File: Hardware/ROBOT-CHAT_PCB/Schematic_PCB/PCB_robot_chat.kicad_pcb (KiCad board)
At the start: 4 copper layers, 67 x 57 mm, 94 parts, among them J1 Conn_01x04, J10 Conn_01x02, J11 Conn_01x02, J12 Conn_01x02, J201 Conn_ST_STDC14, J3 Conn_01x02, J4 Conn_01x02, J5 Conn_01x02, J6 Conn_01x02, J7 Conn_01x06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

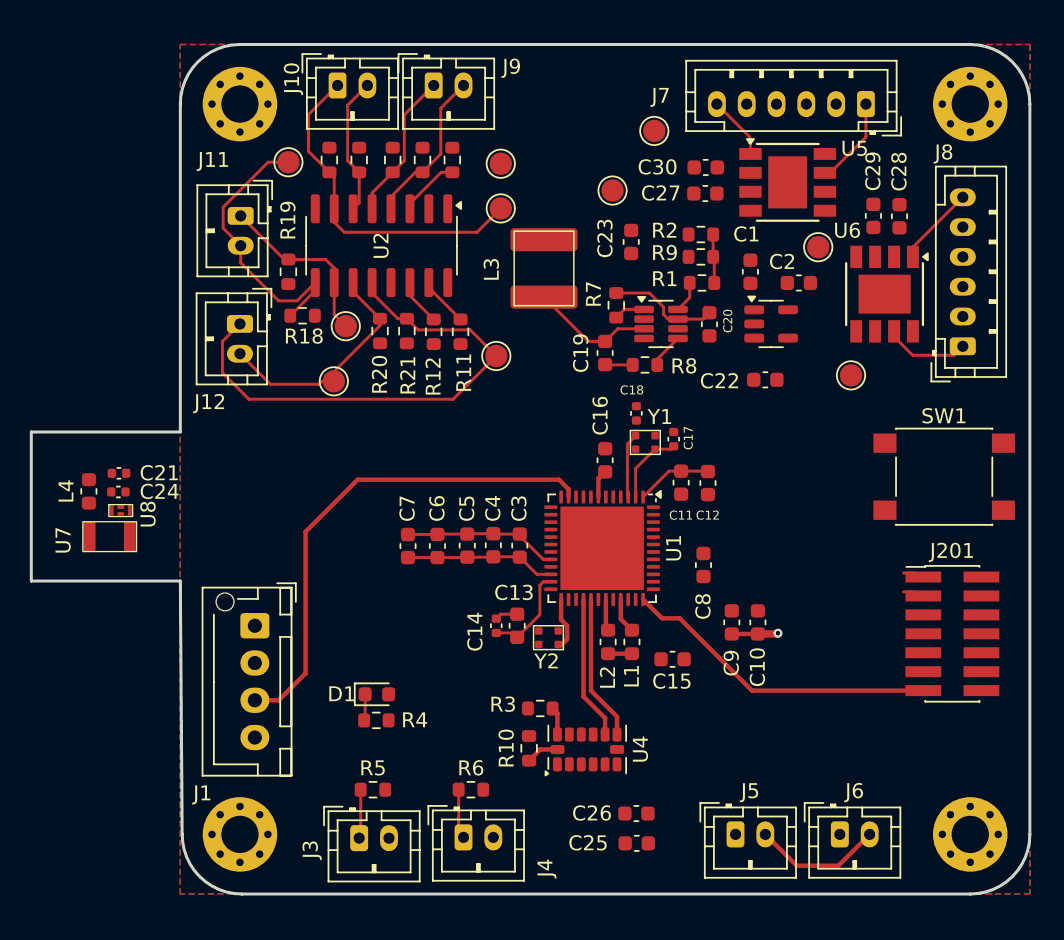
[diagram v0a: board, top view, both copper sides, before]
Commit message: Rerouting avec Mr Fiack
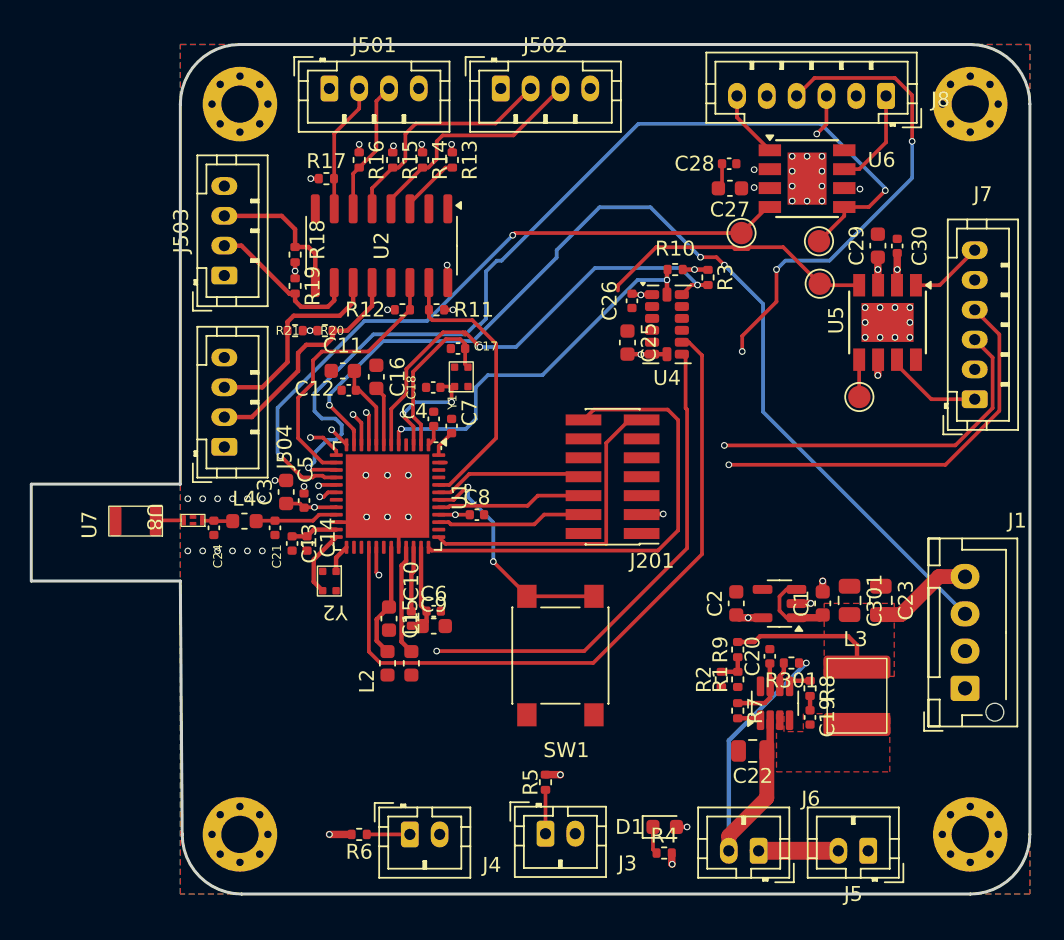
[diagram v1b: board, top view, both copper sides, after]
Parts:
- removed J10, J11, J12, J9: Conn_01x02, Connector_JST:JST_PH_B2B-PH-K_1x02_P2.00mm_Vertical
- removed TP1, TP2, TP3, TP4, TP5, TP6: TestPoint_Small, TestPoint:TestPoint_Pad_D1.5mm
- added C301: 22u, Capacitor_SMD:C_0805_2012Metric, F.Cu at (153.9, 66.3)
- added J501: Conn_01x04, Connector_JST:JST_PH_B4B-PH-K_1x04_P2.00mm_Vertical, F.Cu at (119.0, 31.9)
- added J502: Conn_01x04, Connector_JST:JST_PH_B4B-PH-K_1x04_P2.00mm_Vertical, F.Cu at (130.5, 31.9)
- added J503: Conn_01x04, Connector_JST:JST_PH_B4B-PH-K_1x04_P2.00mm_Vertical, F.Cu at (112.0, 44.5)
- added J504: Conn_01x04, Connector_JST:JST_PH_B4B-PH-K_1x04_P2.00mm_Vertical, F.Cu at (112.0, 56.0)
- added R301: 100k, Resistor_SMD:R_0402_1005Metric, F.Cu at (150.0, 70.5)
- C10, C13, C4, C5, C6, C7, C8: value 100nF -> 100n; footprint Capacitor_SMD:C_0603_1608Metric -> Capacitor_SMD:C_0402_1005Metric
- C12, C28, C30: footprint Capacitor_SMD:C_0603_1608Metric -> Capacitor_SMD:C_0402_1005Metric
- C19, C20: value 0,1uF -> 100n; footprint Capacitor_SMD:C_0603_1608Metric -> Capacitor_SMD:C_0402_1005Metric
- C22: footprint Capacitor_SMD:C_0603_1608Metric -> Capacitor_SMD:C_0805_2012Metric
- C23: value 47uF -> 22u; footprint Capacitor_SMD:C_0603_1608Metric -> Capacitor_SMD:C_0805_2012Metric
- C26: value 0.1uF -> 100n; footprint Capacitor_SMD:C_0603_1608Metric -> Capacitor_SMD:C_0402_1005Metric
- L3: value 4,7uH -> 4.7uH
- R1, R10, R11, R12, R13, R14, R15, R16, R17, R18, R19, R2, R20, R21, R3, R4, R5, R6, R7, R8: footprint Resistor_SMD:R_0603_1608Metric -> Resistor_SMD:R_0402_1005Metric
- R9: value 40,2k -> 40.2k; footprint Resistor_SMD:R_0603_1608Metric -> Resistor_SMD:R_0402_1005Metric
- moved J1 47.8 mm to (161.7, 72.2), turned to 90 degrees
- moved L3 35.5 mm to (150.9, 72.8)
- moved C26 34.4 mm to (139.3, 46.2), turned to -90 degrees
- moved C25 33.6 mm to (139.0, 49.0), turned to -90 degrees
- moved R10 33.6 mm to (142.2, 44.1), turned to 180 degrees
- moved R3 31.0 mm to (144.4, 44.6), turned to -90 degrees
- moved R2 29.9 mm to (145.3, 71.6), turned to 90 degrees
- moved C23 29.3 mm to (156.0, 66.3), turned to -90 degrees
- moved U4 29.0 mm to (141.7, 47.8), turned to 0 degrees
- moved SW1 28.4 mm to (134.5, 70.0), turned to -90 degrees
- moved R7 28.4 mm to (146.4, 73.7)
- moved C19 28.1 mm to (151.2, 74.2), turned to -90 degrees
- moved R1 26.7 mm to (146.4, 71.6), turned to 90 degrees
- moved MP1475DJ-LF-P1 26.6 mm to (148.9, 73.2), turned to 90 degrees
- moved R9 26.5 mm to (146.4, 69.6), turned to 90 degrees
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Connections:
- net Net-(MP1475DJ-LF-P1-BST) renamed /Power/BST
- net Net-(MP1475DJ-LF-P1-FB) renamed /Power/FB
- net Net-(MP1475DJ-LF-P1-PG) renamed /Power/PG
- net Net-(MP1475DJ-LF-P1-SW) renamed /Power/SW
- net Net-(MP1475DJ-LF-P1-VCC) renamed /Power/VCC
- C8 pad 1: +5V -> +3.3V
- J6 pad 1: +7.2V -> /Power/Vbatt+
- J6 pad 2: /Power/Vbatt+ -> +7.2V
- MP1475DJ-LF-P1 pad 6: +5V -> /Power/EN
- U1 pad 12: unconnected-(U1-PA3-Pad12) -> /STM/STATUS_LEDV
- U1 pad 13: /Driver/FWD_2 -> /STM/STATUS_LEDR
- U1 pad 14: /Driver/FWD_1 -> /Multiplexeur/SCL
- U1 pad 15: /Driver/REV_1 -> /Driver/REV_2
- U1 pad 16: /Multiplexeur/SCL -> /Driver/FWD_2
- U1 pad 17: /Driver/REV_2 -> /Driver/Encodeur_2A
- U1 pad 18: /STM/VCP_TX -> /Driver/Encodeur_2B
- U1 pad 36: /STM/VCP_RX -> /STM/VCP_TX
- U1 pad 37: /Driver/Encodeur_2A -> /STM/VCP_RX
- U1 pad 38: /Driver/Encodeur_2B -> unconnected-(U1-PA12-Pad38)
- U1 pad 40: +5V -> +3.3V
- U1 pad 46: /STM/STATUS_LEDV -> /Driver/REV_1
- U1 pad 47: /STM/STATUS_LEDR -> /Driver/FWD_1
- U1 pad 5: /Accéléromètre/SDAacc -> /Accéléromètre/SCLacc
- U1 pad 6: /Accéléromètre/SCLacc -> /Accéléromètre/SDAacc
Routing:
- net /Driver/REV_2: track 0.00 -> 65.3 mm, vias 0 -> 2
- net /Driver/FWD_2: track 0.00 -> 46.3 mm, vias 0 -> 2
- net /Accéléromètre/INTacc1: track 9.66 -> 47.7 mm
- net /STM/UART_TX: track 33.5 -> 67.7 mm, vias 0 -> 3
- net /Driver/Encodeur_2B: track 0.00 -> 33.6 mm, vias 0 -> 4
- net /STM/VCP_TX: track 0.00 -> 31.7 mm
- net /Accéléromètre/SDAacc: track 1.88 -> 32.1 mm, vias 0 -> 2
- net +7.2V: track 0.00 -> 30.0 mm, vias 0 -> 7
- net /Driver/Encodeur_1B: track 0.00 -> 29.4 mm, vias 0 -> 2
- net /Driver/Encodeur_1A: track 0.00 -> 26.4 mm, vias 0 -> 2
- net /Accéléromètre/INTacc2: track 9.79 -> 34.8 mm, vias 0 -> 2
- net /Accéléromètre/SCLacc: track 2.21 -> 26.1 mm, vias 0 -> 2
- net +5V: track 0.00 -> 22.0 mm
- net +3.3V: track 23.1 -> 44.7 mm, vias 0 -> 18
- net /Multiplexeur/SC3: track 34.9 -> 15.6 mm
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- added copper zone on F.Cu, net +5V
- added copper zone on In2.Cu, net +7.2V
- added copper zone on F.Cu, net /Power/SW
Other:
- outline, holes or cut-outs redrawn

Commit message: Routage terminée, début serigraphie
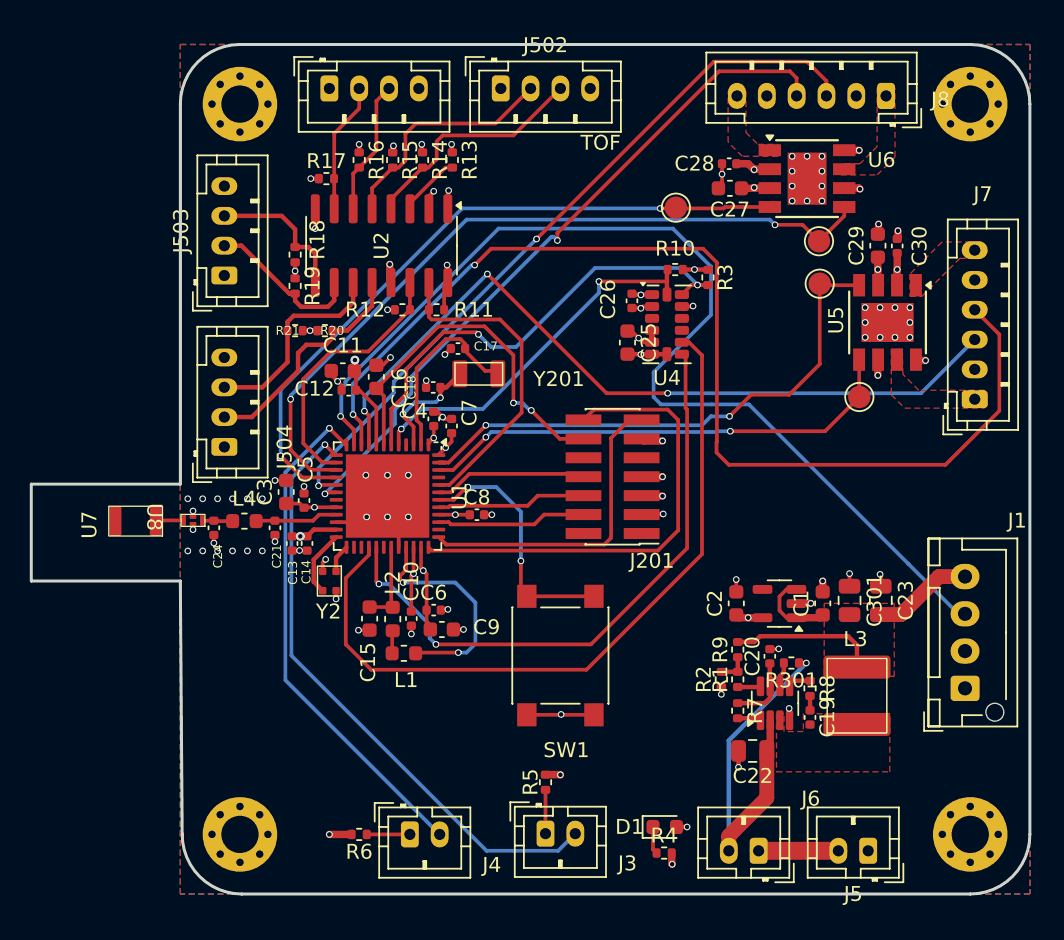
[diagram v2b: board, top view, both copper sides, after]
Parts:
- removed Y1: 32.768kHz, XRCGB32M000F2P01R0:XRCGB32M000F2P01R0
- added Y201: Crystal_Small, ABS07AIG-32.768KHZ-6-D-T:ABS07AIG-32.768KHZ-6-D-T, F.Cu at (129.0, 51.1)
- moved TP9 4.72 mm to (142.2, 40.0)
- moved L2 2.99 mm to (123.2, 67.5)
- moved C15 1.30 mm to (121.7, 67.5)
- moved L1 0.84 mm to (124.0, 69.8), turned to 180 degrees
- moved C9 0.60 mm to (126.5, 68.2)
- moved C6 0.07 mm to (126.0, 67.0)
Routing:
- net /Driver/Encodeur_2A: track 4.03 -> 49.7 mm
- net /Driver/Encodeur_1B: track 29.4 -> 73.9 mm
- net GND: track 16.4 -> 56.1 mm, vias 45 -> 85
- net /STM/STATUS_LEDR: track 2.39 -> 41.1 mm
- net /STM/STATUS_LEDV: track 1.43 -> 34.4 mm
- net /Driver/REV_1: track 2.51 -> 32.8 mm, vias 0 -> 2
- net /Driver/Encodeur_1A: track 26.4 -> 52.5 mm, vias 2 -> 3
- net /STM/NRST: track 3.99 -> 24.6 mm, vias 0 -> 2
- net /Driver/FWD_1: track 19.2 -> 36.9 mm, vias 0 -> 2
- net /Driver/REV_2: track 65.3 -> 51.2 mm
- net /Driver/Encodeur_2B: track 33.6 -> 47.3 mm, vias 4 -> 2
- net Net-(U1-VLXSMPS): track 7.40 -> 15.0 mm, vias 0 -> 2
- net /Driver/Moteur2-: track 6.66 -> 0.00 mm
- net /Driver/Moteur1-: track 6.52 -> 0.00 mm
- net /Accéléromètre/INTacc2: track 34.8 -> 41.3 mm
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- added copper zone on F.Cu, net /Driver/Moteur1+
- added copper zone on F.Cu, net /Driver/Moteur1-
- added copper zone on F.Cu, net /Driver/Moteur2+
- added copper zone on F.Cu, net /Driver/Moteur2-
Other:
- board text added: "TOF"

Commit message: Sérigraphie terminée, PCB v2
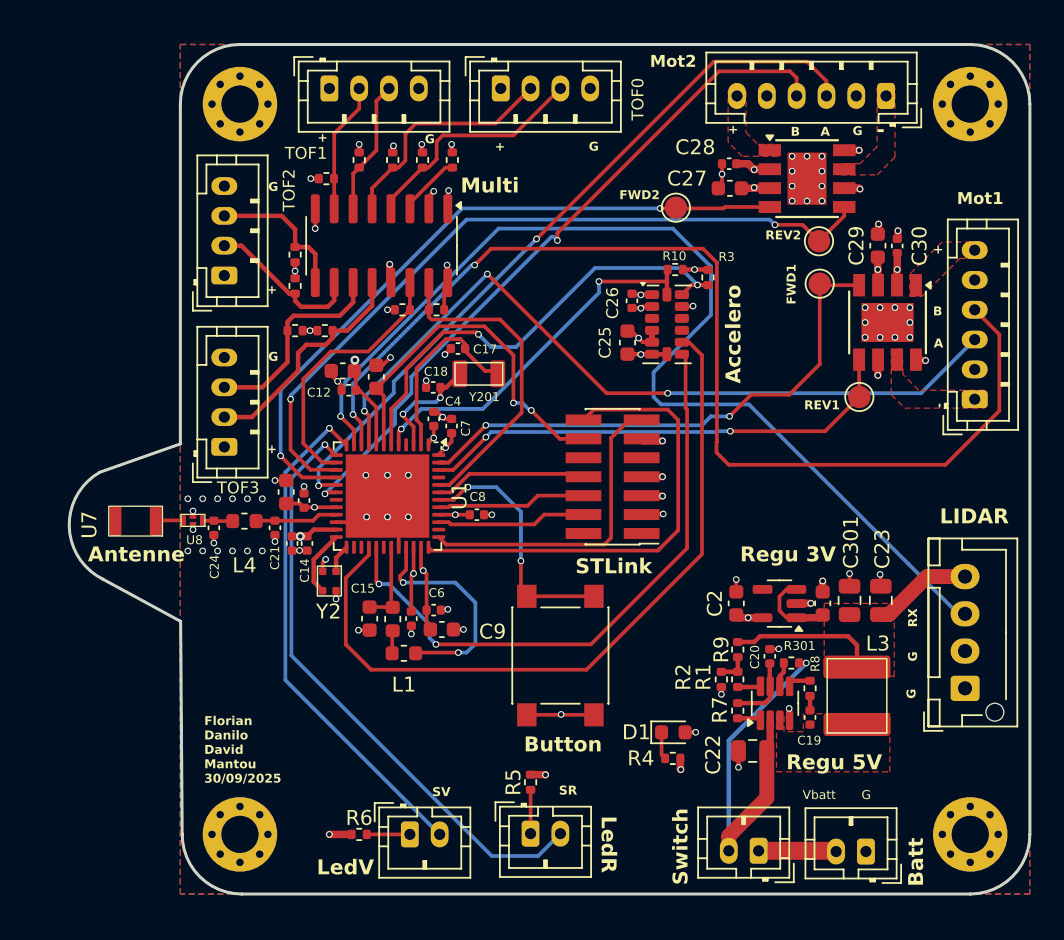
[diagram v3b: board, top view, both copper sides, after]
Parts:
- moved D1 6.38 mm to (142.1, 75.2)
- moved R4 6.38 mm to (142.0, 76.9)
- moved J3 1.00 mm to (132.5, 82.0)
- moved R5 1.00 mm to (132.5, 78.5)
- moved J5 0.16 mm to (155.0, 83.2)
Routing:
- net /STM/STATUS_LEDR: track 41.1 -> 40.4 mm
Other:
- board size 67 x 57 mm -> 64.5 x 57 mm
- board text added: "+"
- board text added: "-"
- board text added: "A"
- board text added: "Accelero"
- board text added: "Antenne"
- board text added: "B"
- board text added: "Batt"
- board text added: "Button"
- board text added: "FWD1"
- board text added: "FWD2"
- board text added: "Florian Danilo David Mantou 30/09/2025"
- board text added: "G"
- board text added: "LIDAR"
- board text added: "LedR"
- board text added: "LedV"
- board text added: "Mot1"
- board text added: "Mot2"
- board text added: "Multi"
- board text added: "REV1"
- board text added: "REV2"
- board text added: "RX"
- board text added: "Regu 3V"
- board text added: "Regu 5V"
- board text added: "SR"
- board text added: "STLink"
- board text added: "SV"
- board text added: "Switch"
- board text added: "TOF0"
- board text added: "TOF1"
- board text added: "TOF2"
- board text added: "TOF3"
- board text added: "Vbatt"
- board text removed: "TOF"

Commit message: Ajout testpoint, PCB v3
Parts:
- added G***: LOGO, LogoENSEA:LogoGrandENSEA, F.Cu at (113.1, 71.9)
- added TP701: TestPoint, TestPoint:TestPoint_Pad_D1.5mm, F.Cu at (134.2, 45.8)
- added TP702: TestPoint, TestPoint:TestPoint_Pad_D1.5mm, F.Cu at (136.8, 45.8)
- added TP703: TestPoint, TestPoint:TestPoint_Pad_D1.5mm, F.Cu at (139.6, 66.0)
- added TP704: TestPoint, TestPoint:TestPoint_Pad_D1.5mm, F.Cu at (140.4, 68.6)
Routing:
- net /Driver/Encodeur_1B: track 73.9 -> 72.2 mm
- net /Accéléromètre/INTacc1: track 50.0 -> 51.1 mm
- net /Accéléromètre/SDAacc: track 31.9 -> 32.9 mm, vias 2 -> 3
- net /Accéléromètre/SCLacc: track 25.2 -> 24.6 mm
- net /Driver/Encodeur_1A: track 52.5 -> 51.9 mm
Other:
- board text added: "Int1"
- board text added: "Int2"
- board text added: "SCL"
- board text added: "SDA"

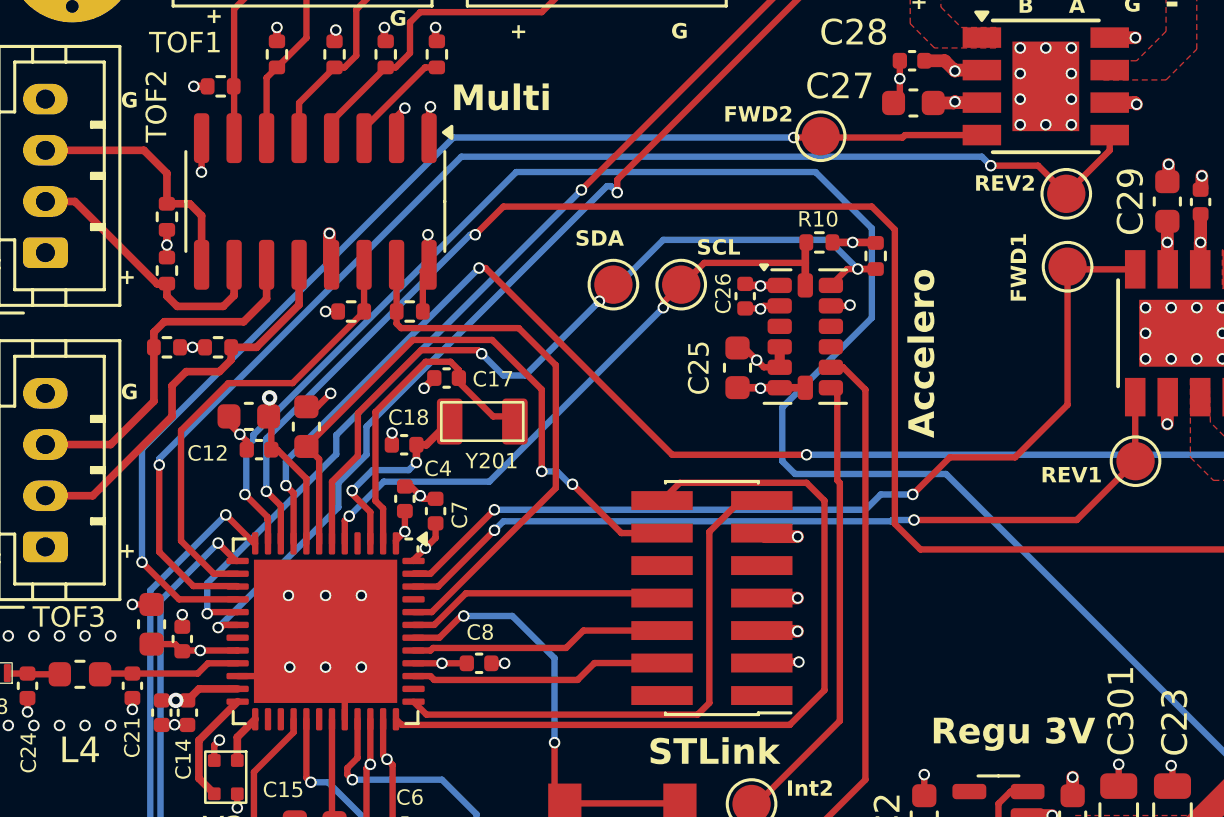
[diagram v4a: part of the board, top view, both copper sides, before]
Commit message: Fixed error pins timers, PCB version 4
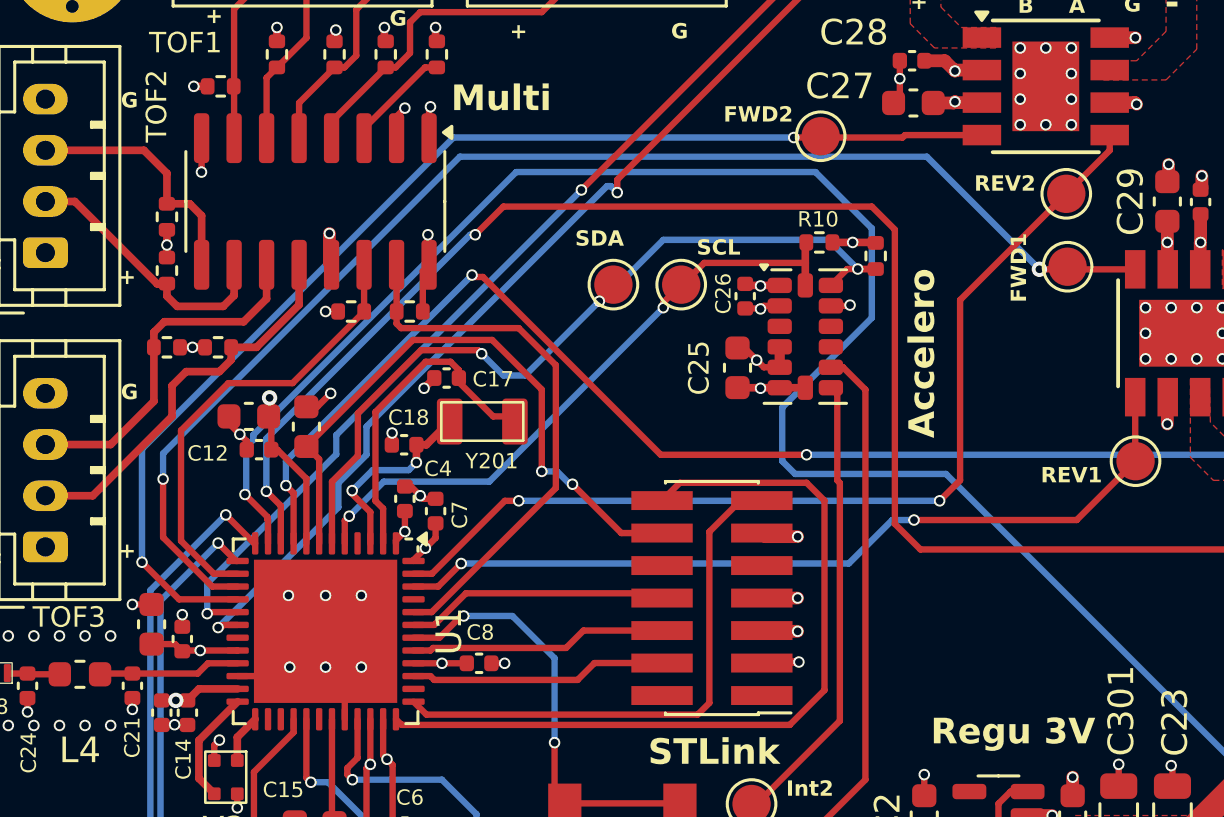
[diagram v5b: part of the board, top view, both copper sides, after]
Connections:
- U1 pad 15: /Driver/REV_2 -> /Driver/FWD_1
- U1 pad 47: /Driver/FWD_1 -> /Driver/REV_2
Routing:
- net /Driver/FWD_1: track 36.9 -> 51.7 mm
- net /Driver/REV_2: track 51.2 -> 38.8 mm

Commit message: PCB final version
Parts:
- moved C18 0.61 mm to (126.0, 51.4)
- moved C17 0.52 mm to (128.2, 49.4)
- moved TP9 0.30 mm to (142.6, 40.0)
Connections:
- U1 pad 10: /Driver/Encodeur_1B -> /Driver/Encodeur_2B
- U1 pad 11: /STM/UART_TX -> /STM/VCP_TX
- U1 pad 12: /STM/STATUS_LEDV -> /STM/VCP_RX
- U1 pad 14: /Multiplexeur/SCL -> /STM/STATUS_LEDV
- U1 pad 15: /Driver/FWD_1 -> unconnected-(U1-PA6-Pad15)
- U1 pad 16: /Driver/FWD_2 -> /Multiplexeur/SCL
- U1 pad 17: /Driver/Encodeur_2A -> /Driver/FWD_1
- U1 pad 18: /Driver/Encodeur_2B -> /Driver/REV_1
- U1 pad 36: /STM/VCP_TX -> /Driver/FWD_2
- U1 pad 37: /STM/VCP_RX -> /Driver/REV_2
- U1 pad 45: unconnected-(U1-PB5-Pad45) -> /Driver/Encodeur_1A
- U1 pad 46: /Driver/REV_1 -> /STM/UART_TX
- U1 pad 47: /Driver/REV_2 -> /Driver/Encodeur_1B
- U1 pad 9: /Driver/Encodeur_1A -> /Driver/Encodeur_2A
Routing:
- net /STM/UART_TX: track 71.6 -> 46.2 mm, vias 1 -> 2
- net /Driver/Encodeur_1B: track 72.2 -> 51.7 mm
- net /Driver/REV_2: track 38.8 -> 49.6 mm
- net /STM/VCP_TX: track 31.7 -> 22.5 mm, vias 0 -> 2
- net /Driver/REV_1: track 32.8 -> 41.9 mm
- net /Driver/FWD_2: track 46.8 -> 52.5 mm
- net /Driver/Encodeur_1A: track 51.7 -> 46.1 mm, vias 3 -> 2
- net /STM/NRST: track 24.6 -> 29.3 mm
- net /Driver/Encodeur_2A: track 49.7 -> 45.7 mm
- net /STM/VCP_RX: track 21.2 -> 25.0 mm, vias 0 -> 2
- net Net-(U1-VLXSMPS): track 15.0 -> 11.7 mm
- net /Driver/Encodeur_2B: track 47.3 -> 44.8 mm
- net /Multiplexeur/SDA: track 21.6 -> 23.8 mm
- net /Accéléromètre/SDAacc: track 32.9 -> 31.1 mm
- net /Accéléromètre/SCLacc: track 24.6 -> 26.0 mm
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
